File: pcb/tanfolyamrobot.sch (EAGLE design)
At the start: 79 parts, among them IC1 STM32F10XRXT6, IC2 7805, IC4 FT232RL, IC5 LD117AS33TR, M1 DRV8833, Q2 BSS123, Q3 BSS123, Q4 BSS123, X1 CSTCE08M, X2 PWR, X6 KUSBVX-BS1N

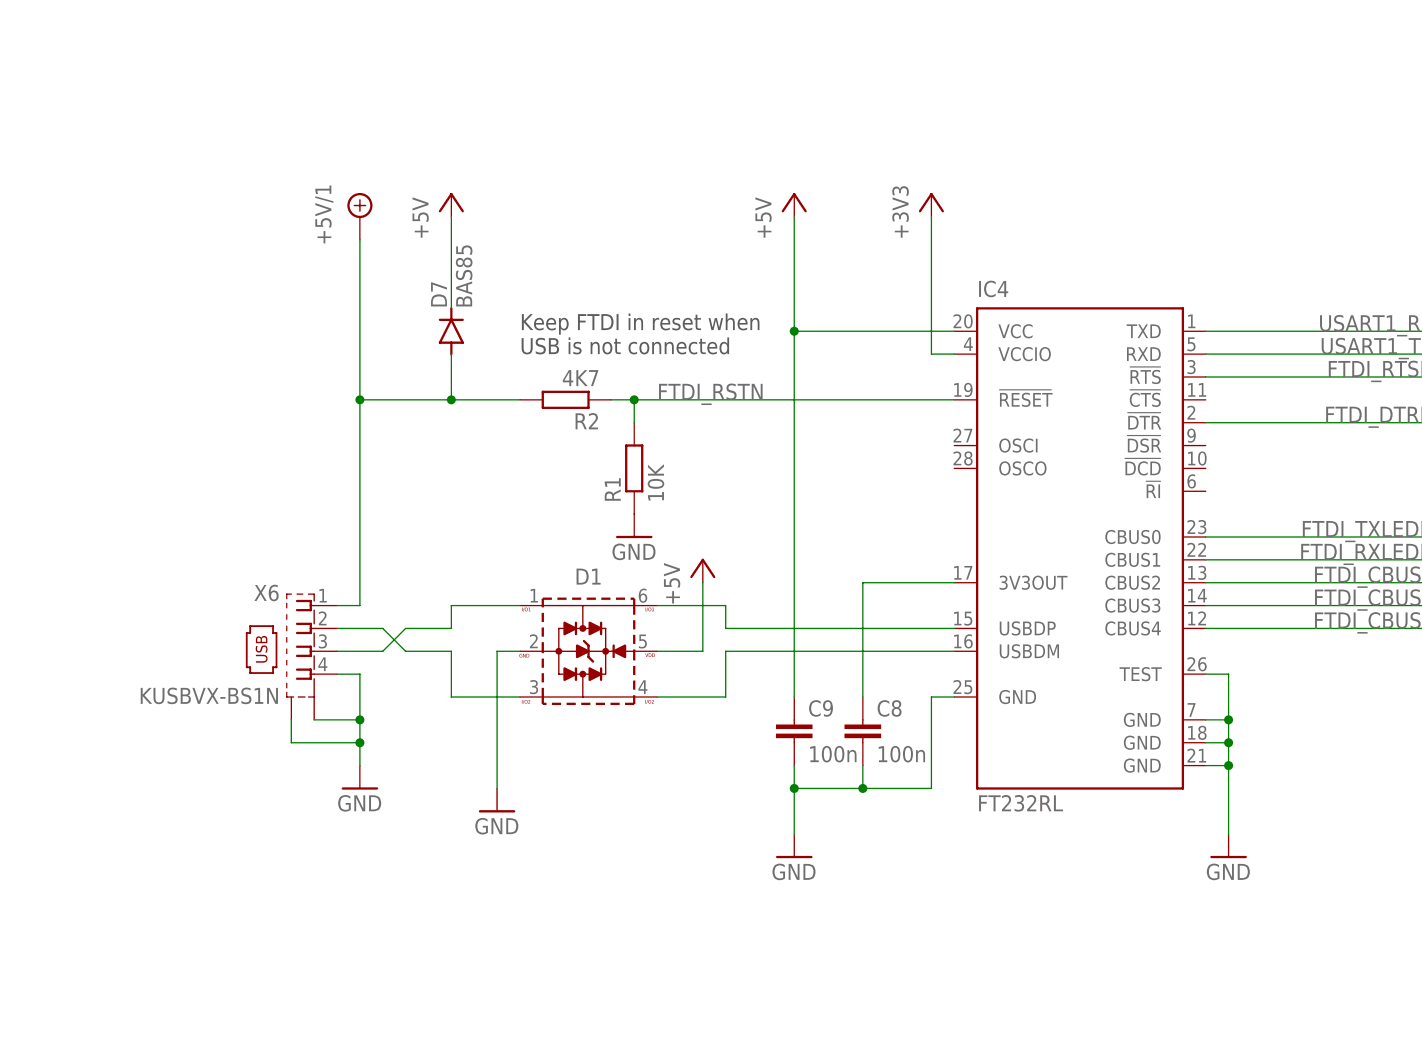
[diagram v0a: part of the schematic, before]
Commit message: added 100n cap to FTDI VCCIO (#1)
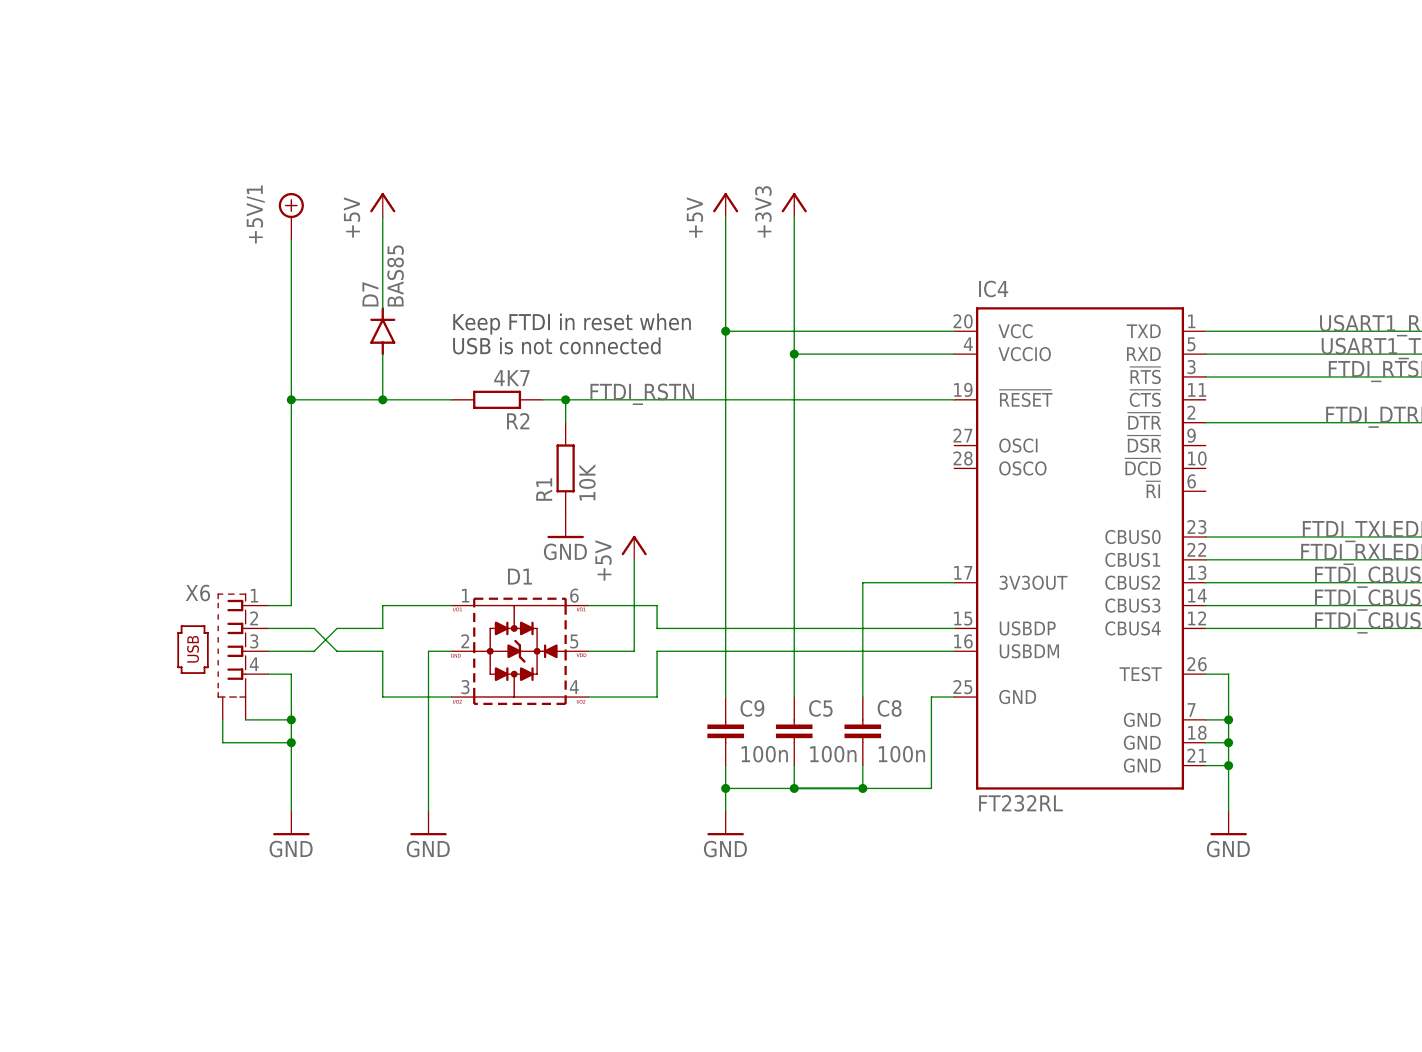
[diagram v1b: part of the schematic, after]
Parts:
- added C5: 100n, rcl:C-EUC0603
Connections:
- net +3V3: now also C5.1
- net GND: now also C5.2
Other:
- moved on the sheet: C9, D1, D7, R1, R2, X6

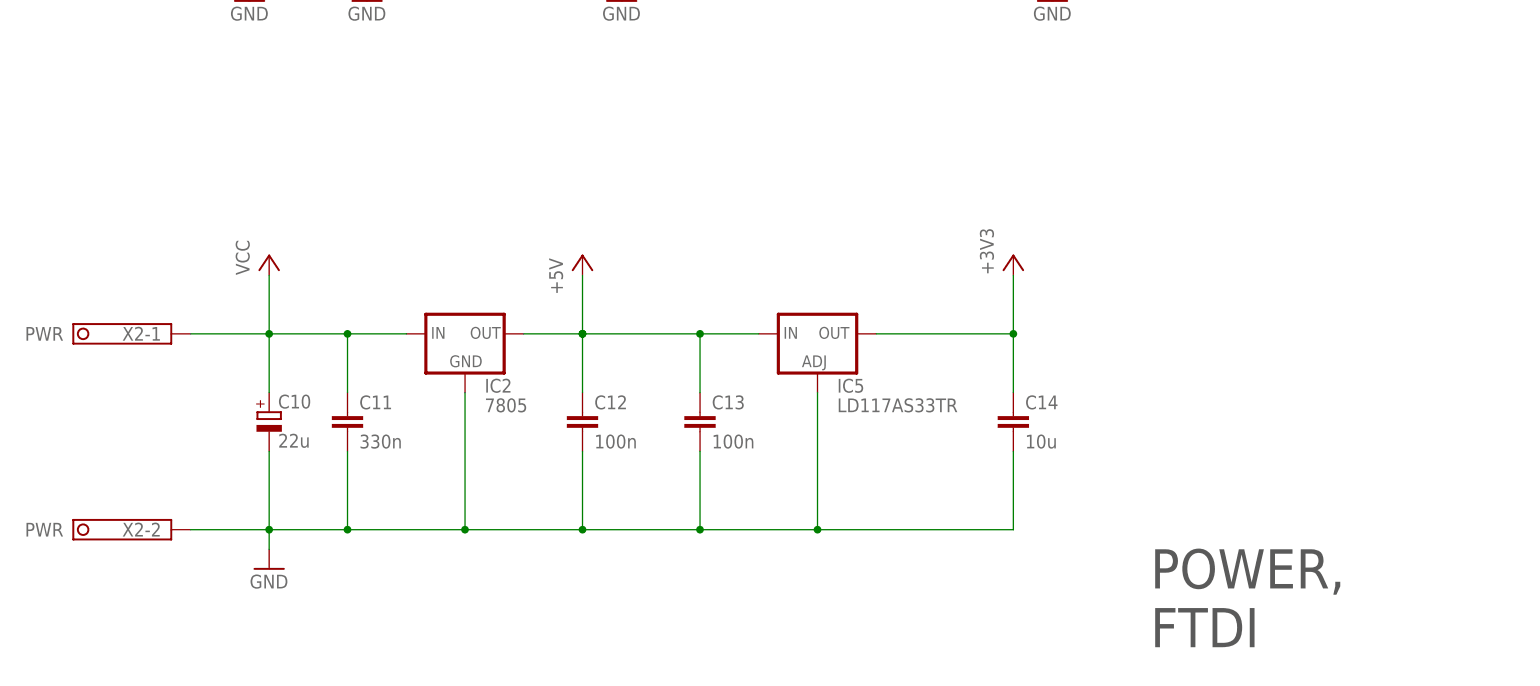
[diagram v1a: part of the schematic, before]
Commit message: added battery polarity protection (#1)
and also fixed some minor DRC errors
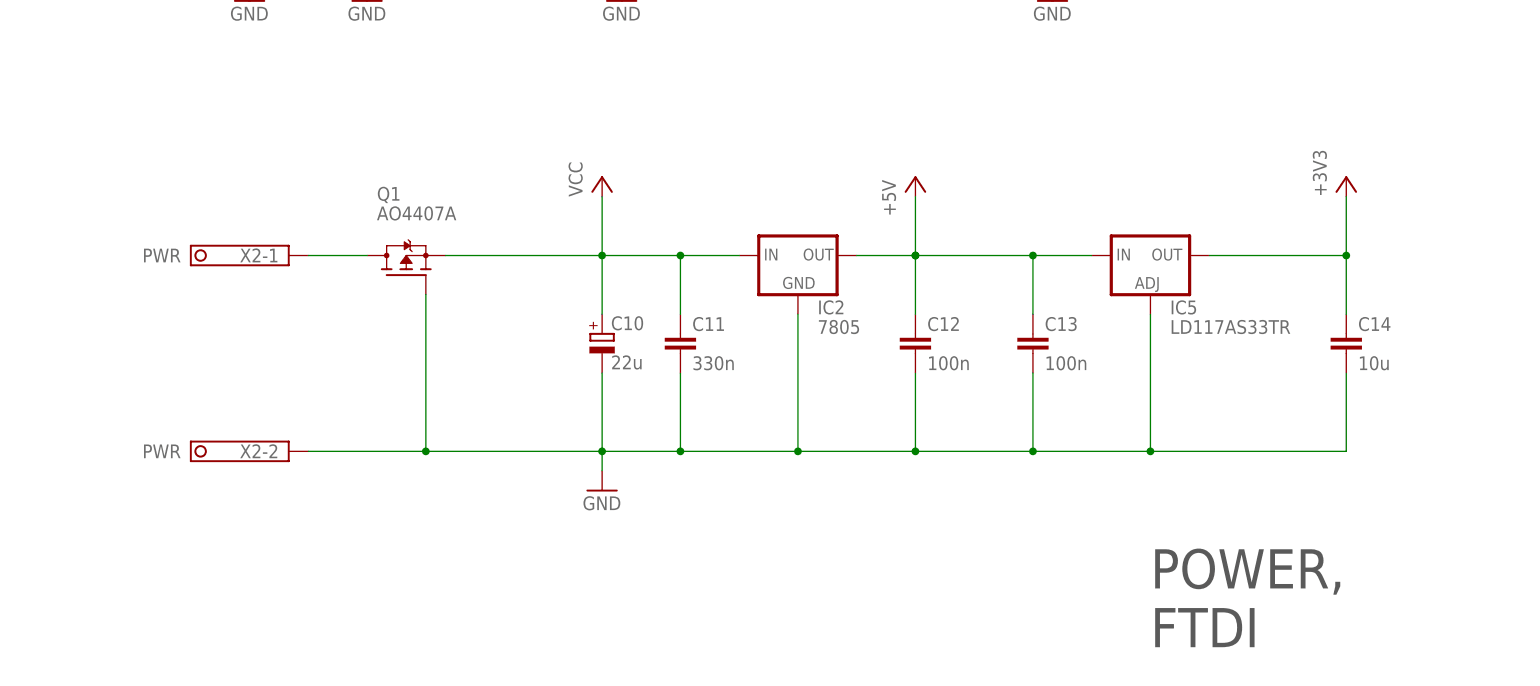
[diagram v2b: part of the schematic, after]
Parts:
- added Q1: AO4407A, transistor-fet:BSO201SP
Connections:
- new net N$3: Q1.D, X2-1.K
- net GND: now also Q1.G
- net VCC: now also Q1.S; no longer X2-1.K
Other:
- moved on the sheet: C10, C11, C12, C13, C14, IC2, IC5, X2-1, X2-2

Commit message: removed todo from schematic (#1)
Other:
- note removed: "TODO: connector type VCC should be 5V?"
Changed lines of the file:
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@@
 <text x="68.58" y="144.78" size="1.778" layer="97">Keep FTDI in reset when
 USB is not connected</text>
-<text x="360.68" y="5.08" size="2.54" layer="150">TODO: connector type
-             VCC should be 5V?</text>
 <text x="429.26" y="227.838" size="1.778" layer="203" rot="MR0">NC</text>
 <text x="429.26" y="222.758" size="1.778" layer="203" rot="MR0">NC</text>

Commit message: added usb power detection (#1)
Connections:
- removed net FTDI_RSTN: IC4.!RESET, R1.2, R2.1, R28.1
- removed net PC9: IC1PORTC_H.PC9
- new net USB_PWR_DET: IC1PORTC_H.PC9, IC4.!RESET, R1.2, R2.1, R28.1
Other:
- moved on the sheet: D1, D7, R1, R2, X6

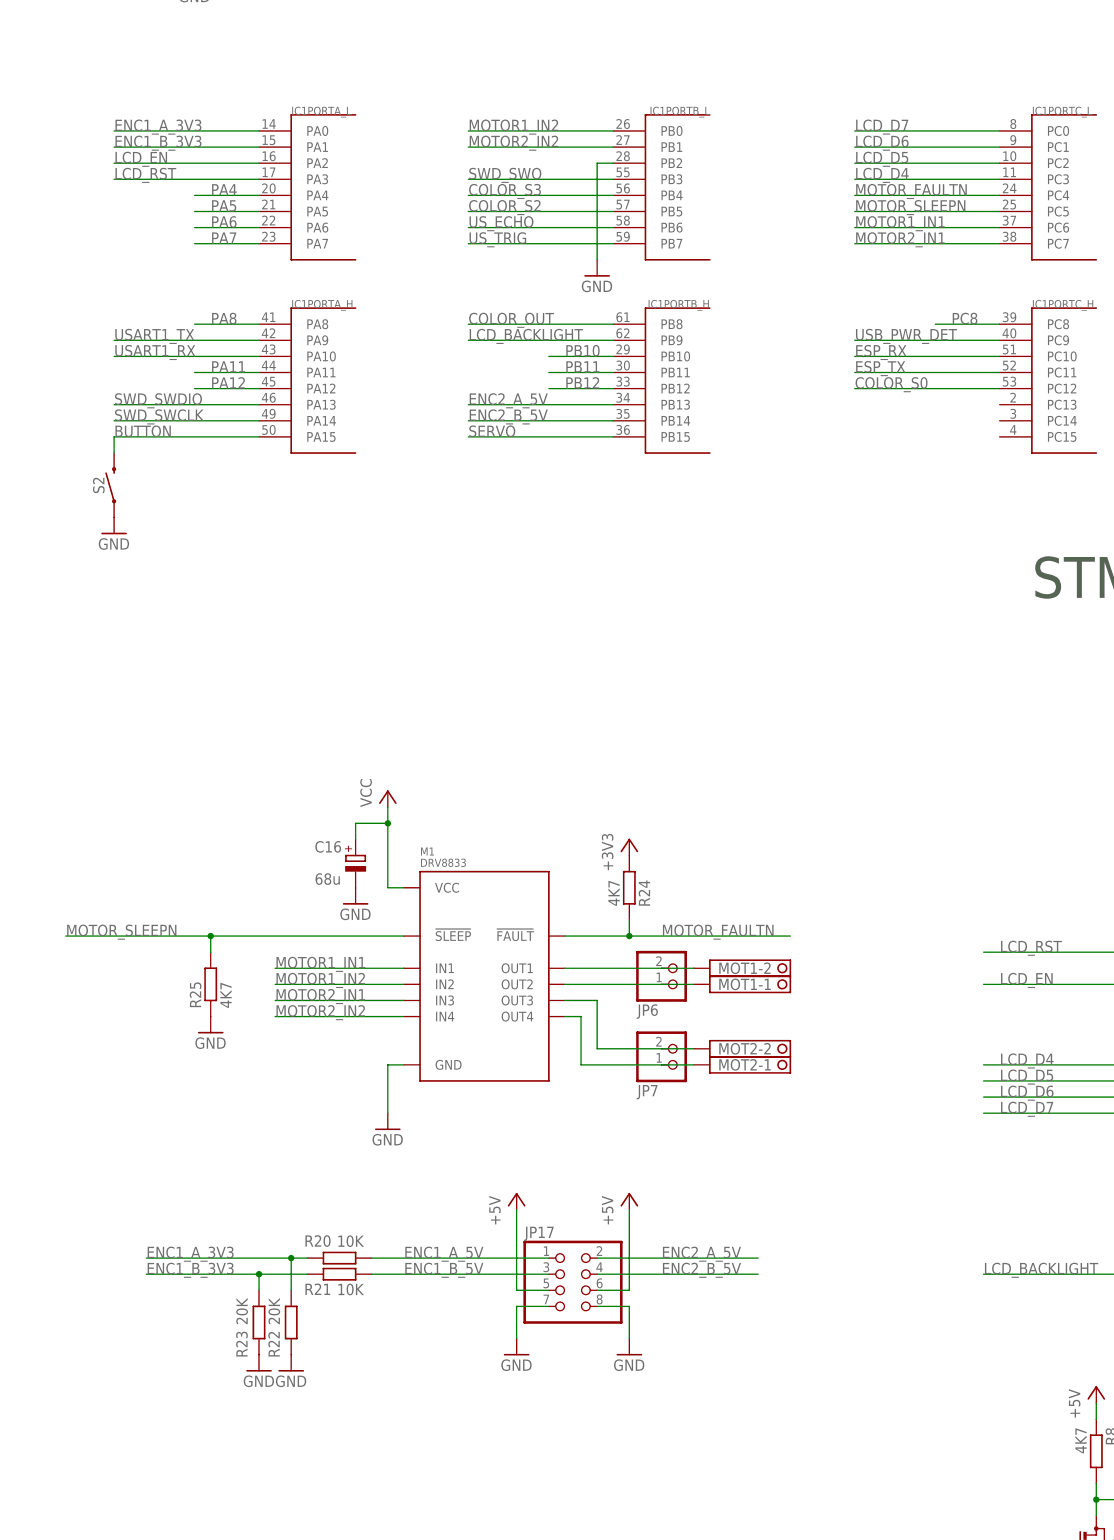
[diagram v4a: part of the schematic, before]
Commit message: fixed encoder stm32 connections (#1)
also had to move lcd pins
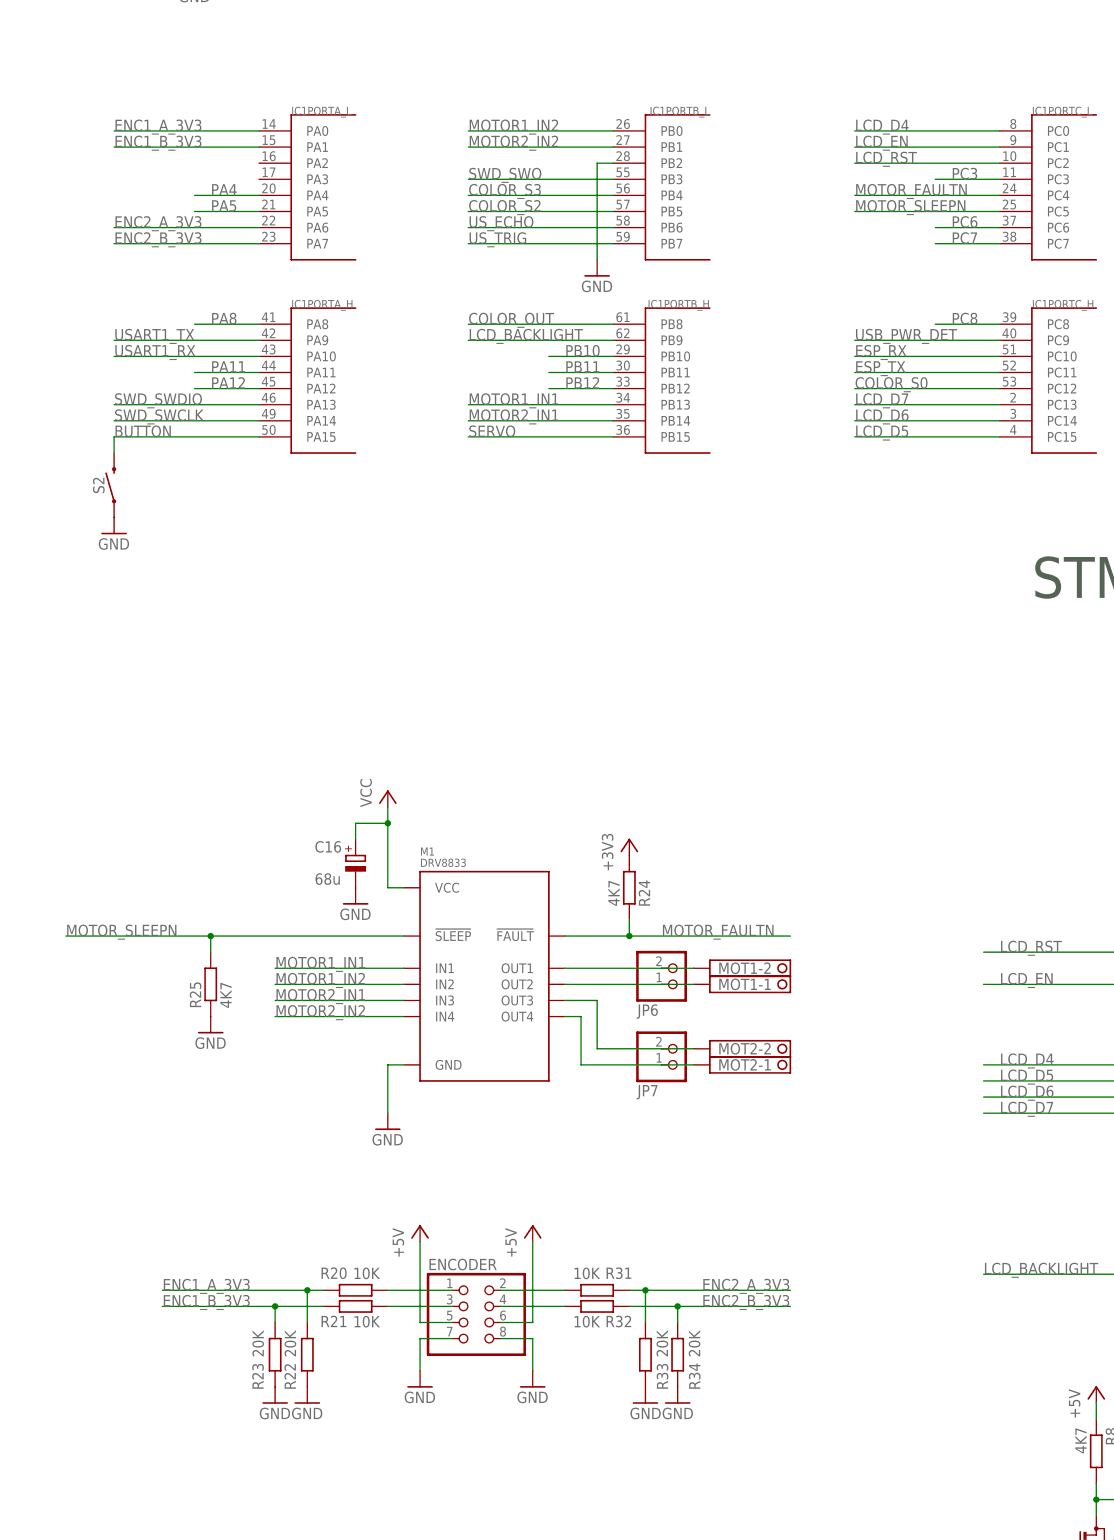
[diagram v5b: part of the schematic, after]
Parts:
- removed JP17: (no value), pinhead:PINHD-2X4/90
- added ENCODER: (no value), pinhead:PINHD-2X4/90
- added R31, R32: 10K, rcl:R-EU_R0603
- added R33, R34: 20K, rcl:R-EU_R0603
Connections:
- removed net PA6: IC1PORTA_L.PA6
- removed net PA7: IC1PORTA_L.PA7
- new net ENC2_A_3V3: IC1PORTA_L.PA6, R31.2, R33.1
- new net ENC2_B_3V3: IC1PORTA_L.PA7, R32.2, R34.1
- new net PC3: IC1PORTC_L.PC3
- new net PC6: IC1PORTC_L.PC6
- new net PC7: IC1PORTC_L.PC7
- net +5V: now also ENCODER.5, ENCODER.6; no longer JP17.5, JP17.6
- net ENC1_A_5V: now also ENCODER.1; no longer JP17.1
- net ENC1_B_5V: now also ENCODER.3; no longer JP17.3
- net ENC2_A_5V: now also ENCODER.2, R31.1; no longer IC1PORTB_H.PB13, JP17.2
- net ENC2_B_5V: now also ENCODER.4, R32.1; no longer IC1PORTB_H.PB14, JP17.4
- net GND: now also ENCODER.7, ENCODER.8, R33.2, R34.2; no longer JP17.7, JP17.8
- net LCD_D4: now also IC1PORTC_L.PC0; no longer IC1PORTC_L.PC3
- net LCD_D5: now also IC1PORTC_H.PC15; no longer IC1PORTC_L.PC2
- net LCD_D6: now also IC1PORTC_H.PC14; no longer IC1PORTC_L.PC1
- net LCD_D7: now also IC1PORTC_H.PC13; no longer IC1PORTC_L.PC0
- net LCD_EN: now also IC1PORTC_L.PC1; no longer IC1PORTA_L.PA2
- net LCD_RST: now also IC1PORTC_L.PC2; no longer IC1PORTA_L.PA3
- net MOTOR1_IN1: now also IC1PORTB_H.PB13; no longer IC1PORTC_L.PC6
- net MOTOR2_IN1: now also IC1PORTB_H.PB14; no longer IC1PORTC_L.PC7
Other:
- note removed: "NC"
- moved on the sheet: R20, R21, R22, R23
